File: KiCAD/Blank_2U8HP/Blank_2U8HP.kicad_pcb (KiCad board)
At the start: 2 copper layers, 40.3 x 84 mm, 4 parts

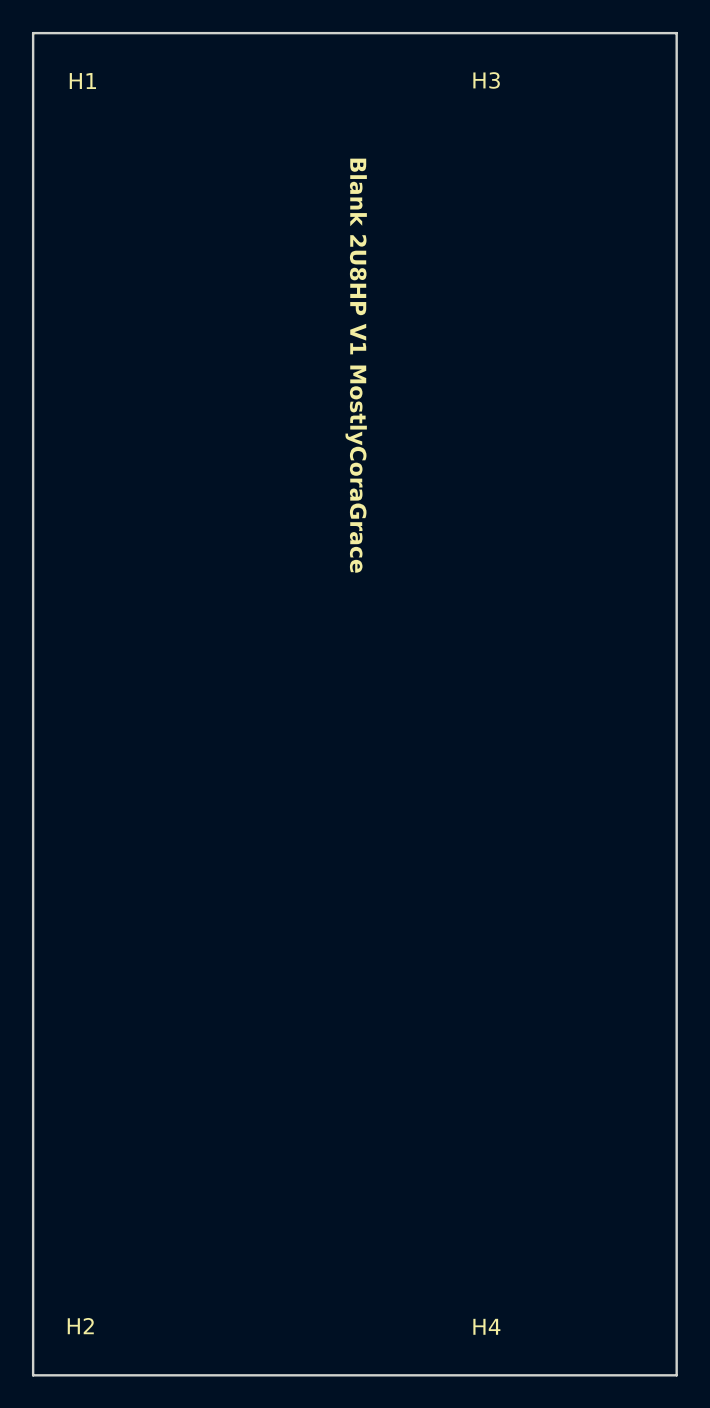
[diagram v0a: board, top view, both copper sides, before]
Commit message: removed all front silkscreen, and flipped most modules, to make the boards 'cleaner'.
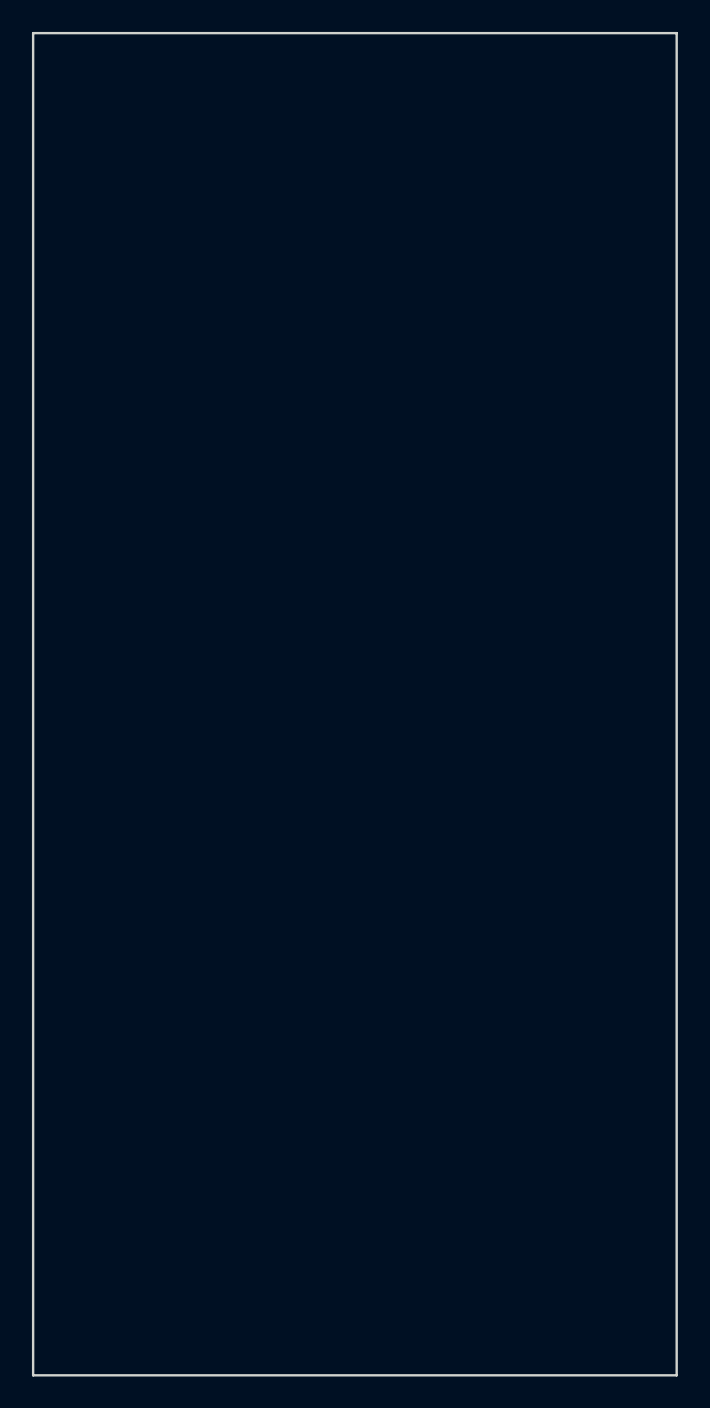
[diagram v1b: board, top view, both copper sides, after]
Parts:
- H1, H2, H3, H4: moved to B.Cu
- turned H1 to 180 degrees
- turned H2 to 180 degrees
- turned H3 to 180 degrees
- turned H4 to 180 degrees

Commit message: added copper fills to every module, to maybe possibly increase structural rigidity.
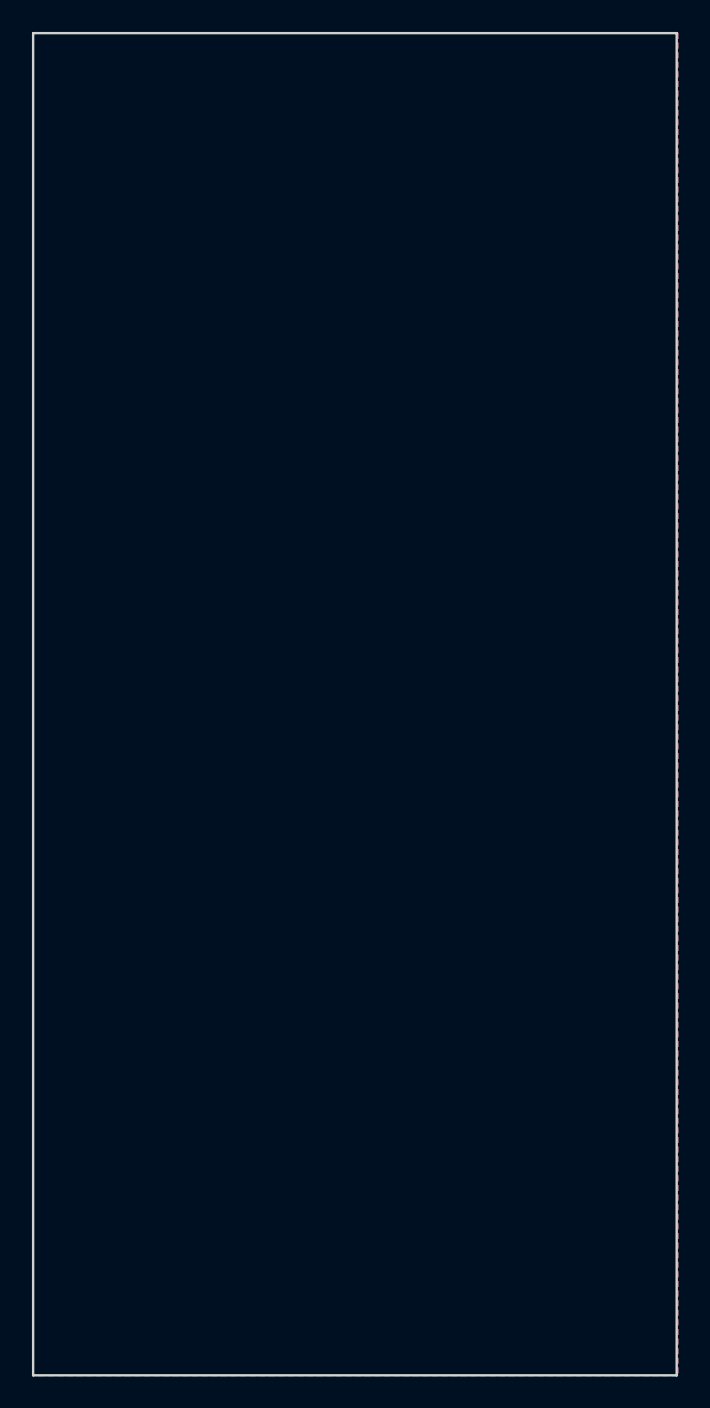
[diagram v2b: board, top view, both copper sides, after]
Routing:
- added copper zone on B.Cu, net (none)
- added copper zone on F.Cu, net (none)
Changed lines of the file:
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@@
+		)
+	)
+	(zone
+		(net 0)
+		(net_name "")
+		(layers "F&B.Cu")
+		(hatch edge 0.5)
+		(connect_pads
+			(clearance 0.5)
+		)
+		(min_thickness 0.25)
+		(filled_areas_thickness no)
+		(fill yes
+			(thermal_gap 0.5)
+			(thermal_bridge_width 0.5)
+			(island_removal_mode 1)
+			(island_area_min 10)
+		)
+		(polygon
+			(pts
+				(xy 0 2.413) (xy 40.386 2.413) (xy 40.386 86.487) (xy 0 86.487)
+			)
 		)
 	)
